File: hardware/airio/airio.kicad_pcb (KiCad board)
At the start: 2 copper layers, 42 x 24 mm, 18 parts, among them J1 LiPo 1S, SW1 TS-1187A-B-A-B, U1 XIAO nRF52840, U2 BMP581, U3 LSM6DSV16X

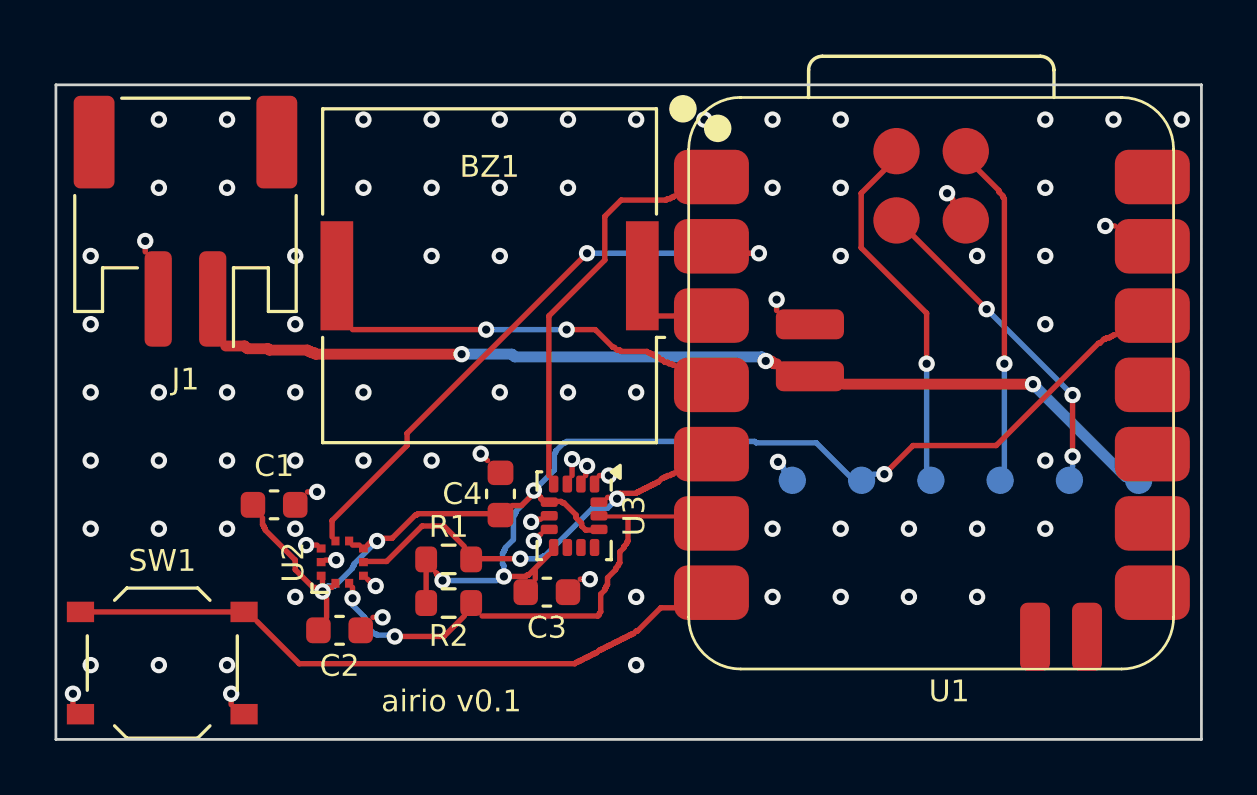
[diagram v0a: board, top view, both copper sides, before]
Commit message: airio: remove tracks, vias and ground pours; keep placement
Leaves the placed footprints, board outline, antenna keepout and rules
so the board can be routed by hand.

Co-Authored-By: Claude Opus 5.5 (1M context) <noreply@anthropic.com>
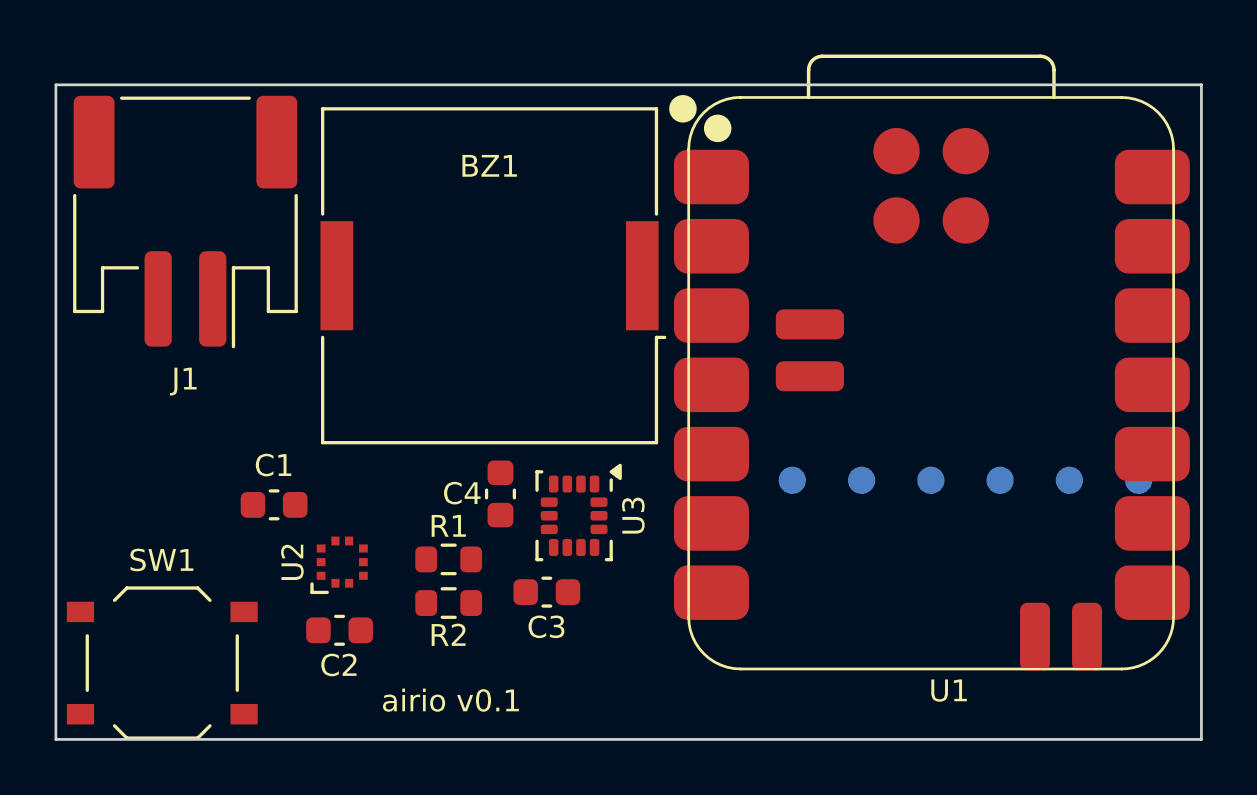
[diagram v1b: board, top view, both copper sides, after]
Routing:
- net +3V3: track 49.2 -> 0.00 mm, vias 6 -> 0
- net /VBAT: track 32.2 -> 0.00 mm, vias 3 -> 0
- net /BTN: track 21.8 -> 0.00 mm
- net /BARO_INT: track 21.0 -> 0.00 mm, vias 2 -> 0
- net /I2C_SCL: track 16.4 -> 0.00 mm, vias 2 -> 0
- net /IMU_INT1: track 13.2 -> 0.00 mm
- net /I2C_SDA: track 13.1 -> 0.00 mm, vias 2 -> 0
- net /BUZZ_B: track 12.3 -> 0.00 mm, vias 2 -> 0
- net /SWDIO: track 12.2 -> 0.00 mm, vias 1 -> 0
- net /SWCLK: track 11.3 -> 0.00 mm, vias 1 -> 0
- net /XIAO_RST: track 10.9 -> 0.00 mm, vias 3 -> 0
- net GND: track 7.39 -> 0.00 mm, vias 85 -> 0
- net /BUZZ_A: track 0.60 -> 0.00 mm
- removed copper zone on B.Cu, net GND
- removed copper zone on F.Cu, net GND

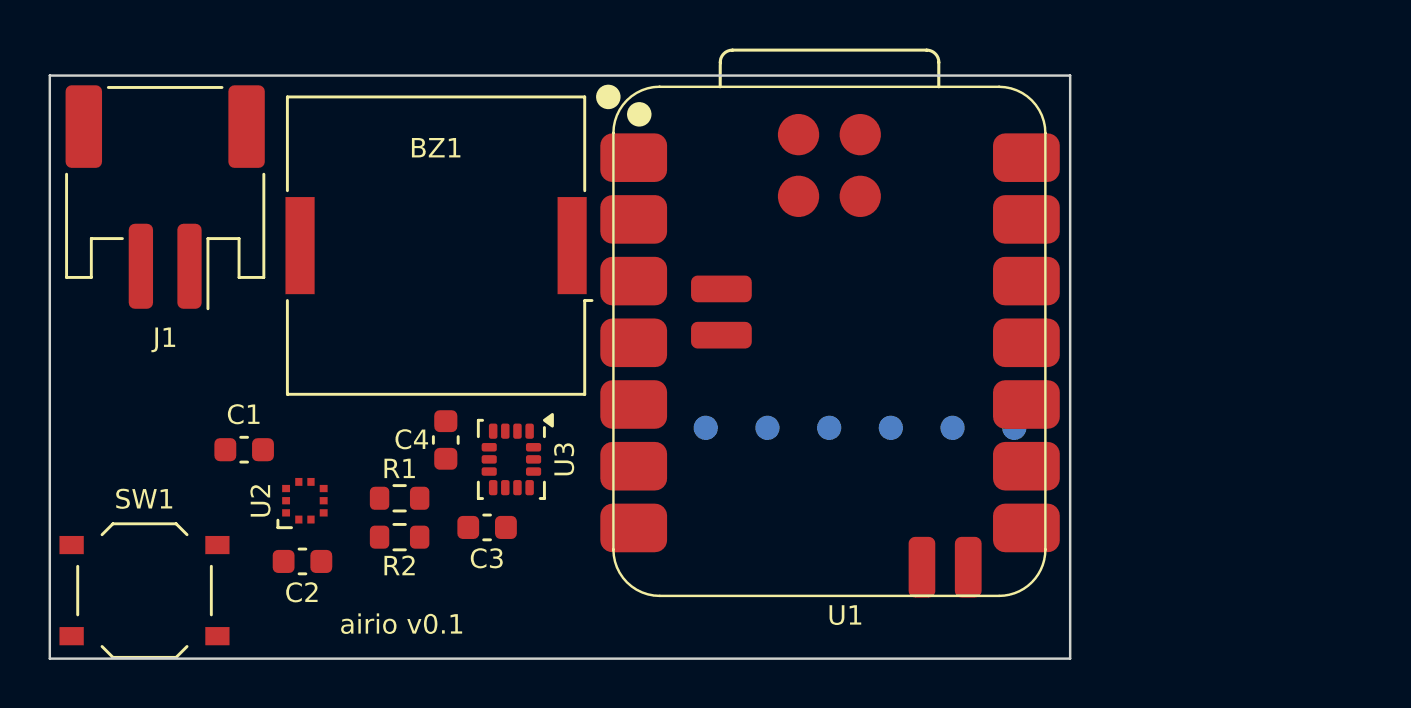
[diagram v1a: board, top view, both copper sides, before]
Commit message: airio: add GPS, screen and spare I2C JST-PH ports
- Schematic: J2 GPS UART (GND, 3V3, GPS TX to D7, GPS RX from NFC1),
  J3 screen (GND, 3V3, VBAT, SCK D8, MOSI D10, CS D9, DISP NFC2, pin 8 NC),
  J4 spare I2C (GND, 3V3, SDA, SCL). B4B/B8B-PH-K vertical THT, pin 1 GND.
- Board widened from 42 to 54 mm; ports in a 12 mm strip on the left,
  placement only. Antenna keepout moved with the XIAO.
- ERC 0 errors; DRC with schematic parity has no footprint errors.
- Pin map and parts tables updated; BMP581 back in stock.

Co-Authored-By: Claude Opus 5.5 (1M context) <noreply@anthropic.com>
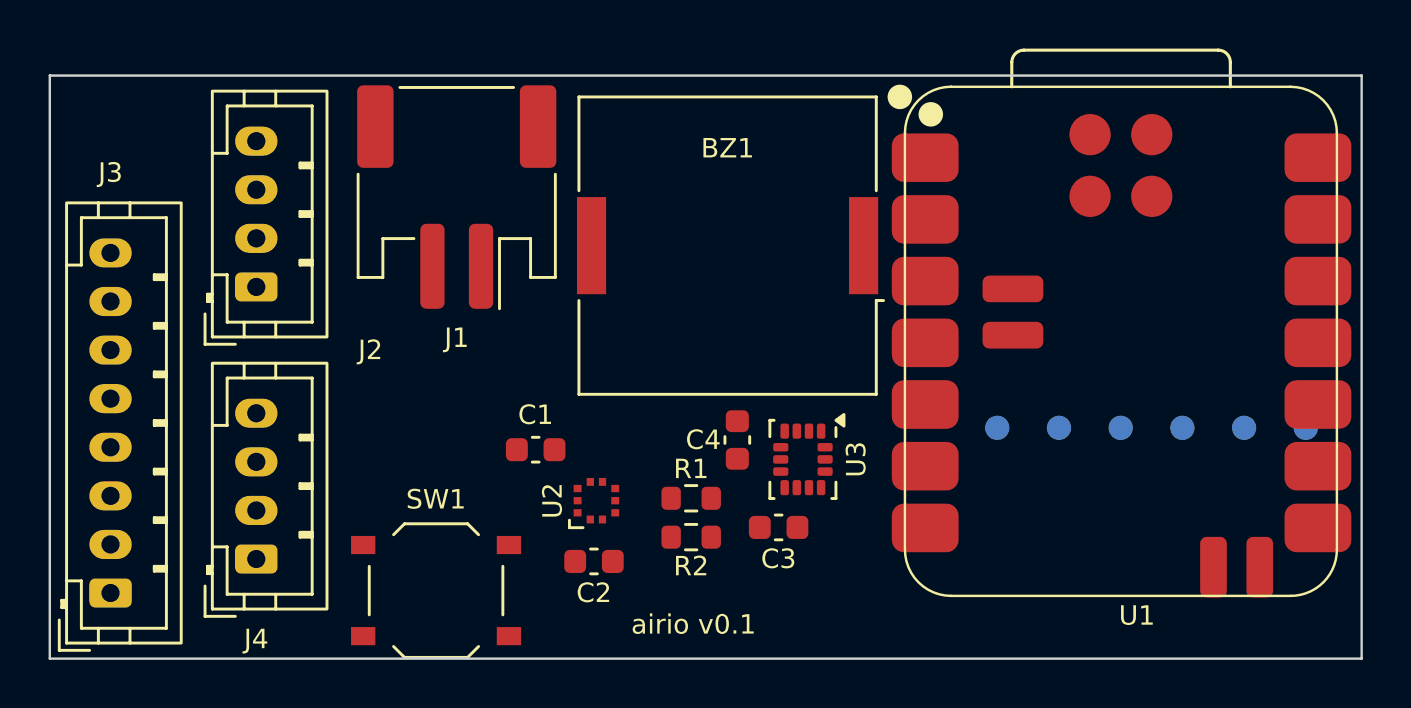
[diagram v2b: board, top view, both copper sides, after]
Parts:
- added J2: GPS, Connector_JST:JST_PH_B4B-PH-K_1x04_P2.00mm_Vertical, F.Cu at (8.50, 8.70)
- added J3: SCREEN, Connector_JST:JST_PH_B8B-PH-K_1x08_P2.00mm_Vertical, F.Cu at (2.50, 21.3)
- added J4: I2C, Connector_JST:JST_PH_B4B-PH-K_1x04_P2.00mm_Vertical, F.Cu at (8.50, 19.9)
- moved U1 12.0 mm to (35.2, 21.5)
- moved C1 12.0 mm to (20.0, 15.4)
- moved C3 12.0 mm to (30.0, 18.6)
- moved C4 12.0 mm to (28.3, 15.0)
- moved J1 12.0 mm to (16.8, 5.00)
- moved SW1 12.0 mm to (15.9, 21.2)
- moved TP1 12.0 mm to (44.1, 14.5)
- moved TP2 12.0 mm to (46.6, 14.5)
- moved TP3 12.0 mm to (49.2, 14.5)
- moved TP4 12.0 mm to (51.7, 14.5)
- moved TP5 12.0 mm to (41.5, 14.5)
- moved TP6 12.0 mm to (39.0, 14.5)
- moved U2 12.0 mm to (22.5, 17.5)
- moved U3 12.0 mm to (31.0, 15.8)
- moved BZ1 12.0 mm to (27.9, 7.00)
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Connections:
- U1 pad 10: unconnected-(U1-D9-Pad10) -> /SCR_CS
- U1 pad 11: unconnected-(U1-D10-Pad11) -> /SCR_MOSI
- U1 pad 21: unconnected-(U1-NFC1-Pad21) -> /GPS_RX
- U1 pad 22: unconnected-(U1-NFC2-Pad22) -> /SCR_DISP
- U1 pad 8: unconnected-(U1-D7-Pad8) -> /GPS_TX
- U1 pad 9: unconnected-(U1-D8-Pad9) -> /SCR_SCK
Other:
- board size 42 x 24 mm -> 54 x 24 mm

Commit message: airio: switch U1 to the XIAO nRF52840 Plus
The NFC pads carrying GPS_RX and SCR_DISP sat inside the antenna keepout,
so they could not be routed. The XIAO Plus has the same chip and outline
plus D11-D19 on half-pitch castellations away from the antenna.

- New symbol XIAO_nRF52840_Plus: GPS_RX on D12 (P0.19), SCR_DISP on D11
  (P0.15); SWD/RST/GND/battery pads renumbered 24-29 to Seeed's order.
- Footprint XIAO-nRF52840-Plus-SMD from Seeed's library, rotated so the
  main pads land where the standard XIAO's did; swapped in place on the
  board.
- ERC 0 errors; DRC with schematic parity has no footprint errors.
- Pin map and parts tables updated (Plus is not on LCSC).

Co-Authored-By: Claude Opus 5.5 (1M context) <noreply@anthropic.com>
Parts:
- U1: value XIAO nRF52840 -> XIAO nRF52840 Plus; footprint airio:XIAO-nRF52840-SMD -> airio:XIAO-nRF52840-Plus-SMD
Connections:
- U1 pad 15: /SWDIO -> /SCR_DISP
- U1 pad 16: /SWCLK -> /GPS_RX
- U1 pad 17: /XIAO_RST -> unconnected-(U1-D13-Pad17)
- U1 pad 18: GND -> unconnected-(U1-D14-Pad18)
- U1 pad 19: /VBAT -> unconnected-(U1-D15-Pad19)
- U1 pad 20: GND -> unconnected-(U1-D16_VBAT-Pad20)
- U1 pad 21: /GPS_RX -> unconnected-(U1-D17-Pad21)
- U1 pad 22: /SCR_DISP -> unconnected-(U1-D18-Pad22)

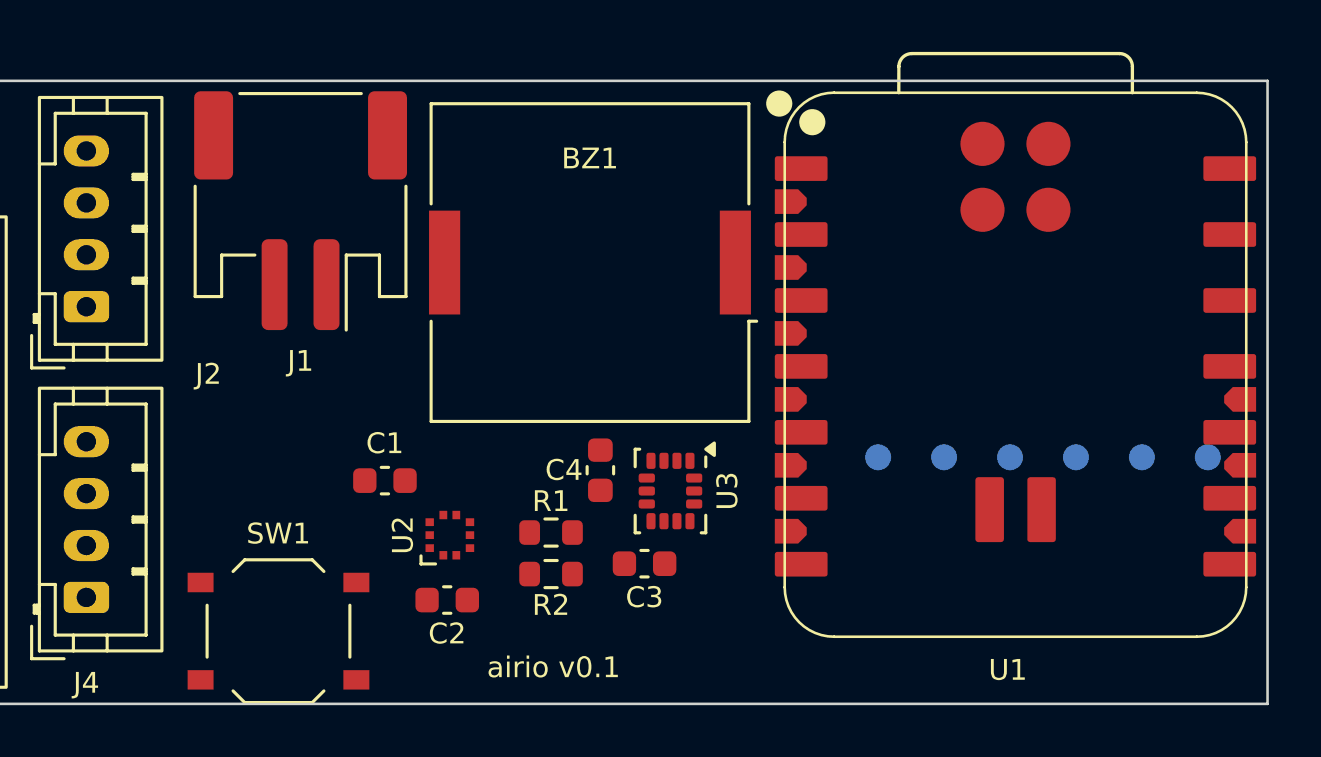
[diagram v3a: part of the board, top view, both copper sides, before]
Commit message: airio: back to the standard XIAO, add a TCA9534 I/O expander
- U1 is the standard XIAO nRF52840 again (on LCSC, JLC can place it).
- GPS_RX moves to D1; D6 becomes EXP_INT from the expander.
- U4 TCA9534PWR at 0x20 carries BTN (P0, R4 pull-up), BARO_INT (P1) and
  SCR_DISP (P2); its open-drain INT (R3 pull-up) still wakes the XIAO
  from System OFF. C5 decouples it. NFC pads unused.
- Board: U1 swapped back, U4/R3/R4/C5 placed near the sensors.
- ERC 0 errors; DRC with schematic parity has no footprint errors.
- Pin map and parts tables updated.

Co-Authored-By: Claude Opus 5.5 (1M context) <noreply@anthropic.com>
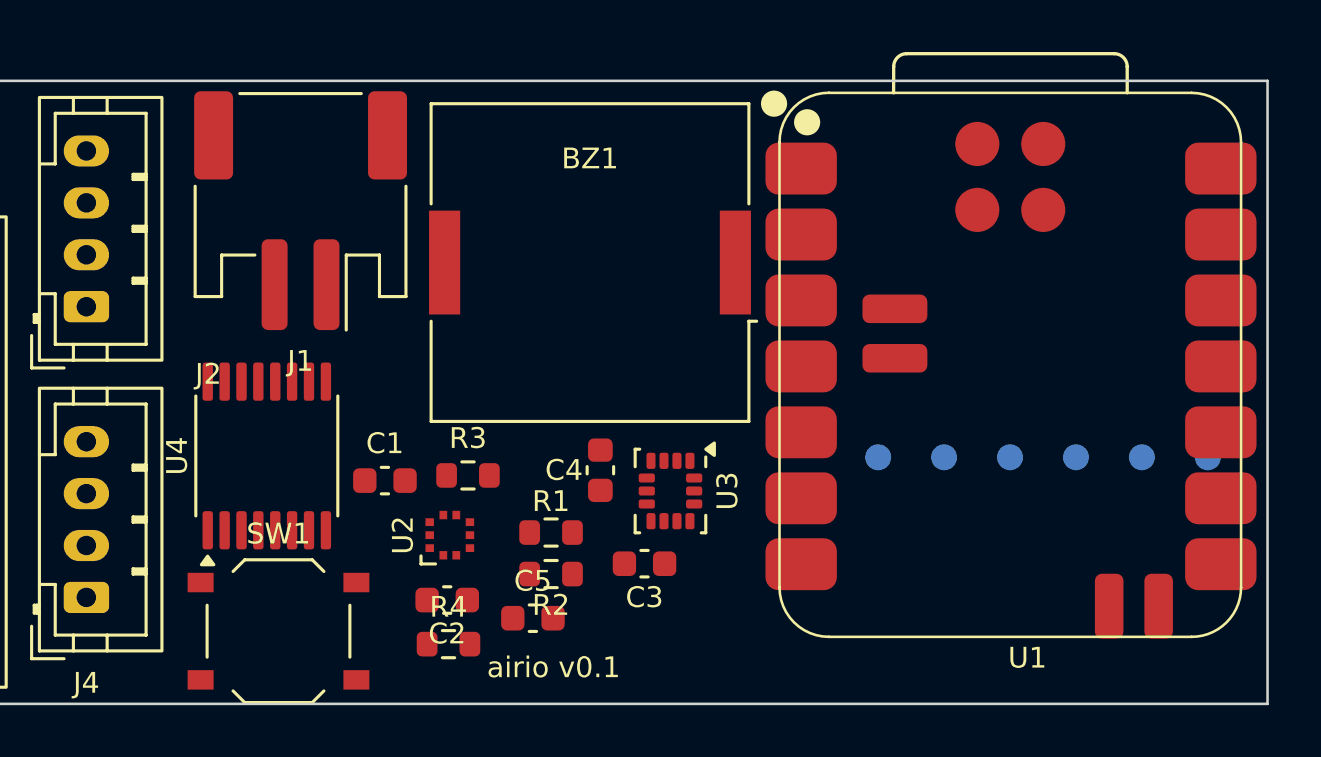
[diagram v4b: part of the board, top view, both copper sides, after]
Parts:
- added C5: 100n, Capacitor_SMD:C_0603_1608Metric, F.Cu at (25.7, 20.7)
- added R3: 10k, Resistor_SMD:R_0603_1608Metric, F.Cu at (23.2, 15.2)
- added R4: 10k, Resistor_SMD:R_0603_1608Metric, F.Cu at (22.4, 21.7)
- added U4: TCA9534PWR, Package_SO:TSSOP-16_4.4x5mm_P0.65mm, F.Cu at (15.4, 14.4)
- U1: value XIAO nRF52840 Plus -> XIAO nRF52840; footprint airio:XIAO-nRF52840-Plus-SMD -> airio:XIAO-nRF52840-SMD
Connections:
- U1 pad 15: /SCR_DISP -> /SWDIO
- U1 pad 16: /GPS_RX -> /SWCLK
- U1 pad 17: unconnected-(U1-D13-Pad17) -> /XIAO_RST
- U1 pad 18: unconnected-(U1-D14-Pad18) -> GND
- U1 pad 19: unconnected-(U1-D15-Pad19) -> /VBAT
- U1 pad 2: /BARO_INT -> /GPS_RX
- U1 pad 20: unconnected-(U1-D16_VBAT-Pad20) -> GND
- U1 pad 7: /BTN -> /EXP_INT
